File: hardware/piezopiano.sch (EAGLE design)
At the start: 71 parts, among them J1 CON2, J4 JST-PH-2-SMT-SE, Q1 DMN3404L, Q2 DMN3404L, Q3 DMN3404L, Q4 DMN3404L, Q5 DMN3404L, Q6 DMN3404L, Q7 DMN3404L, Q8 DMN3404L, U1 MEGA48A-AU, U2 CH340E_MSOP10, U3 TP4333, Y1 830069392

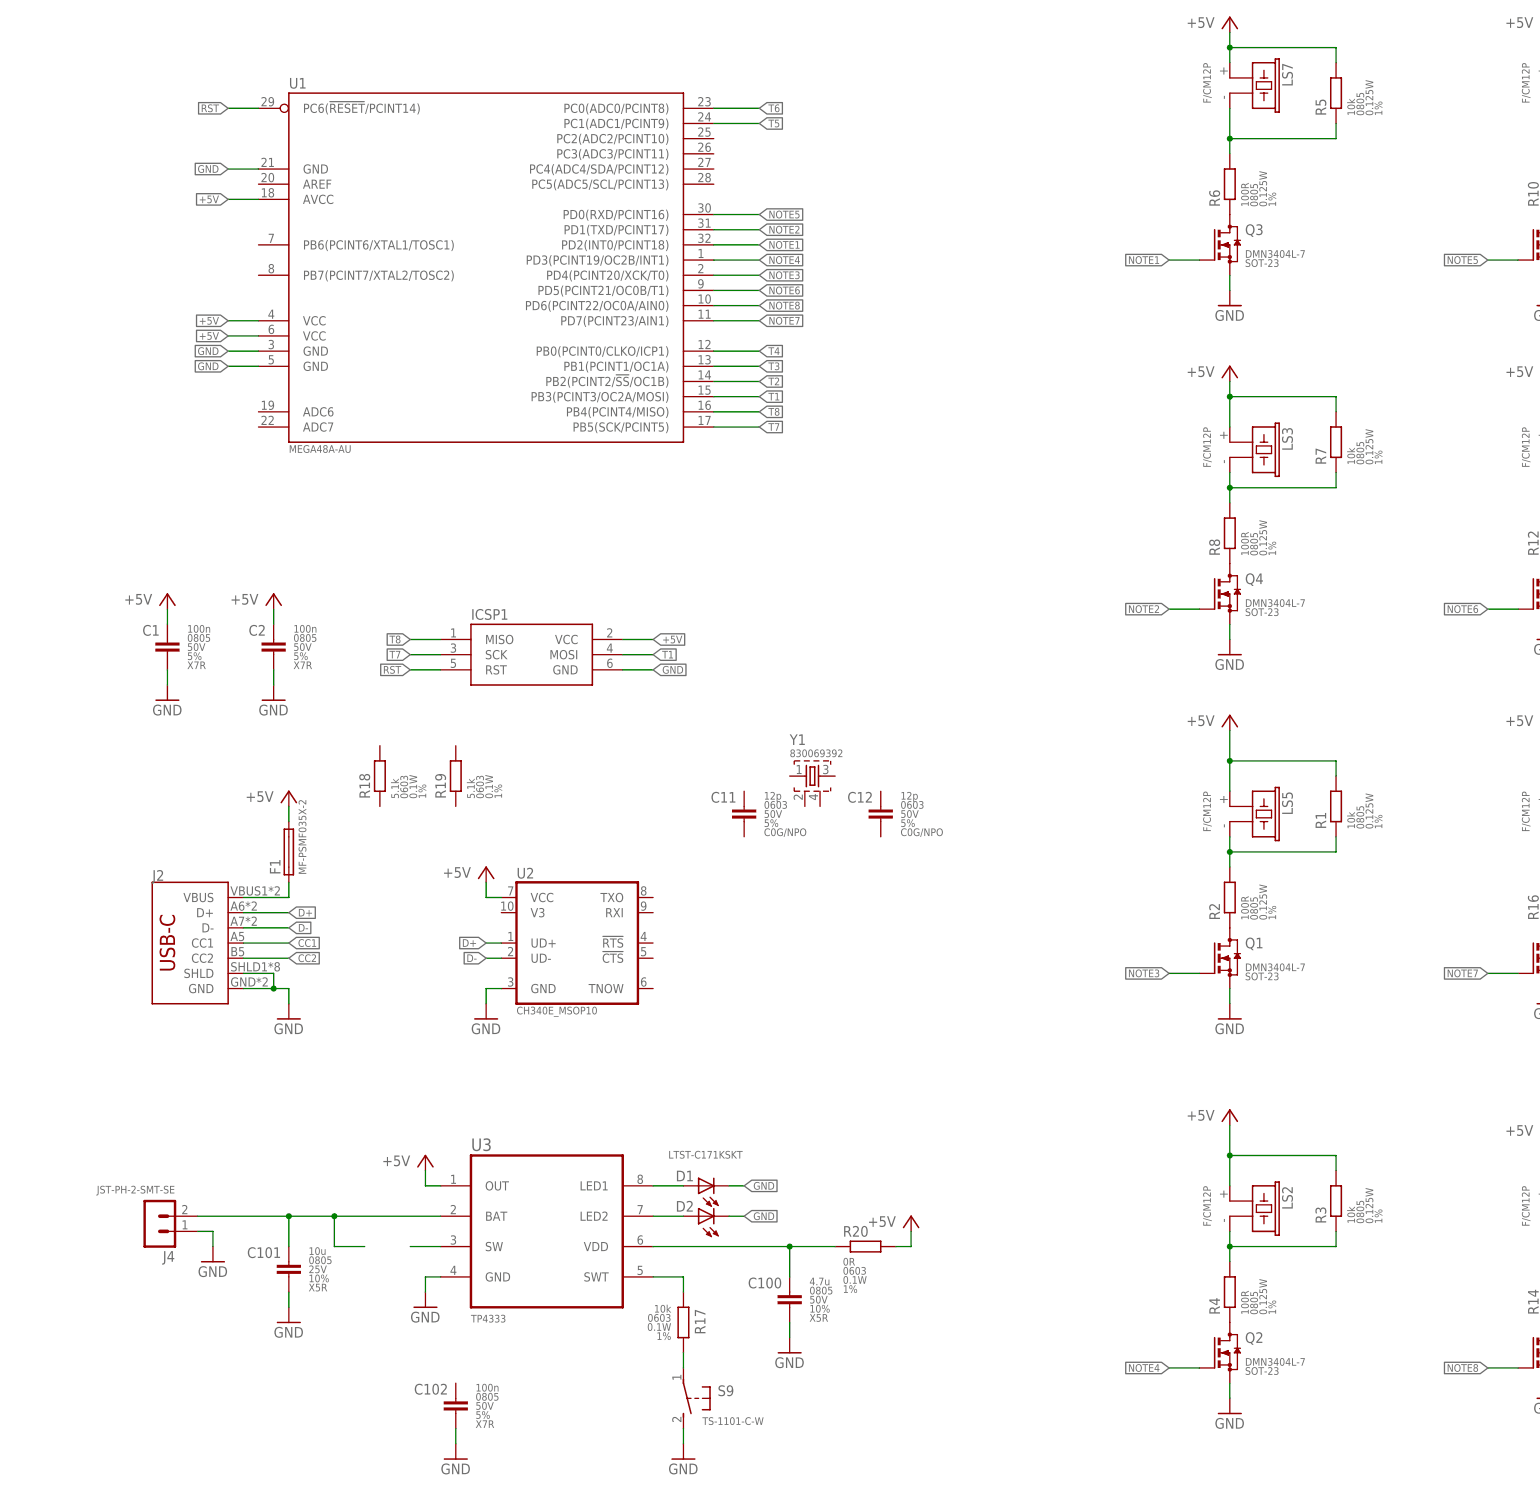
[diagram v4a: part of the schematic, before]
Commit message: Changed to 328 for Arduino support
Changed to ATmega328
Fixed radius from outline
Corrected CH340E
Changed Pinout 328
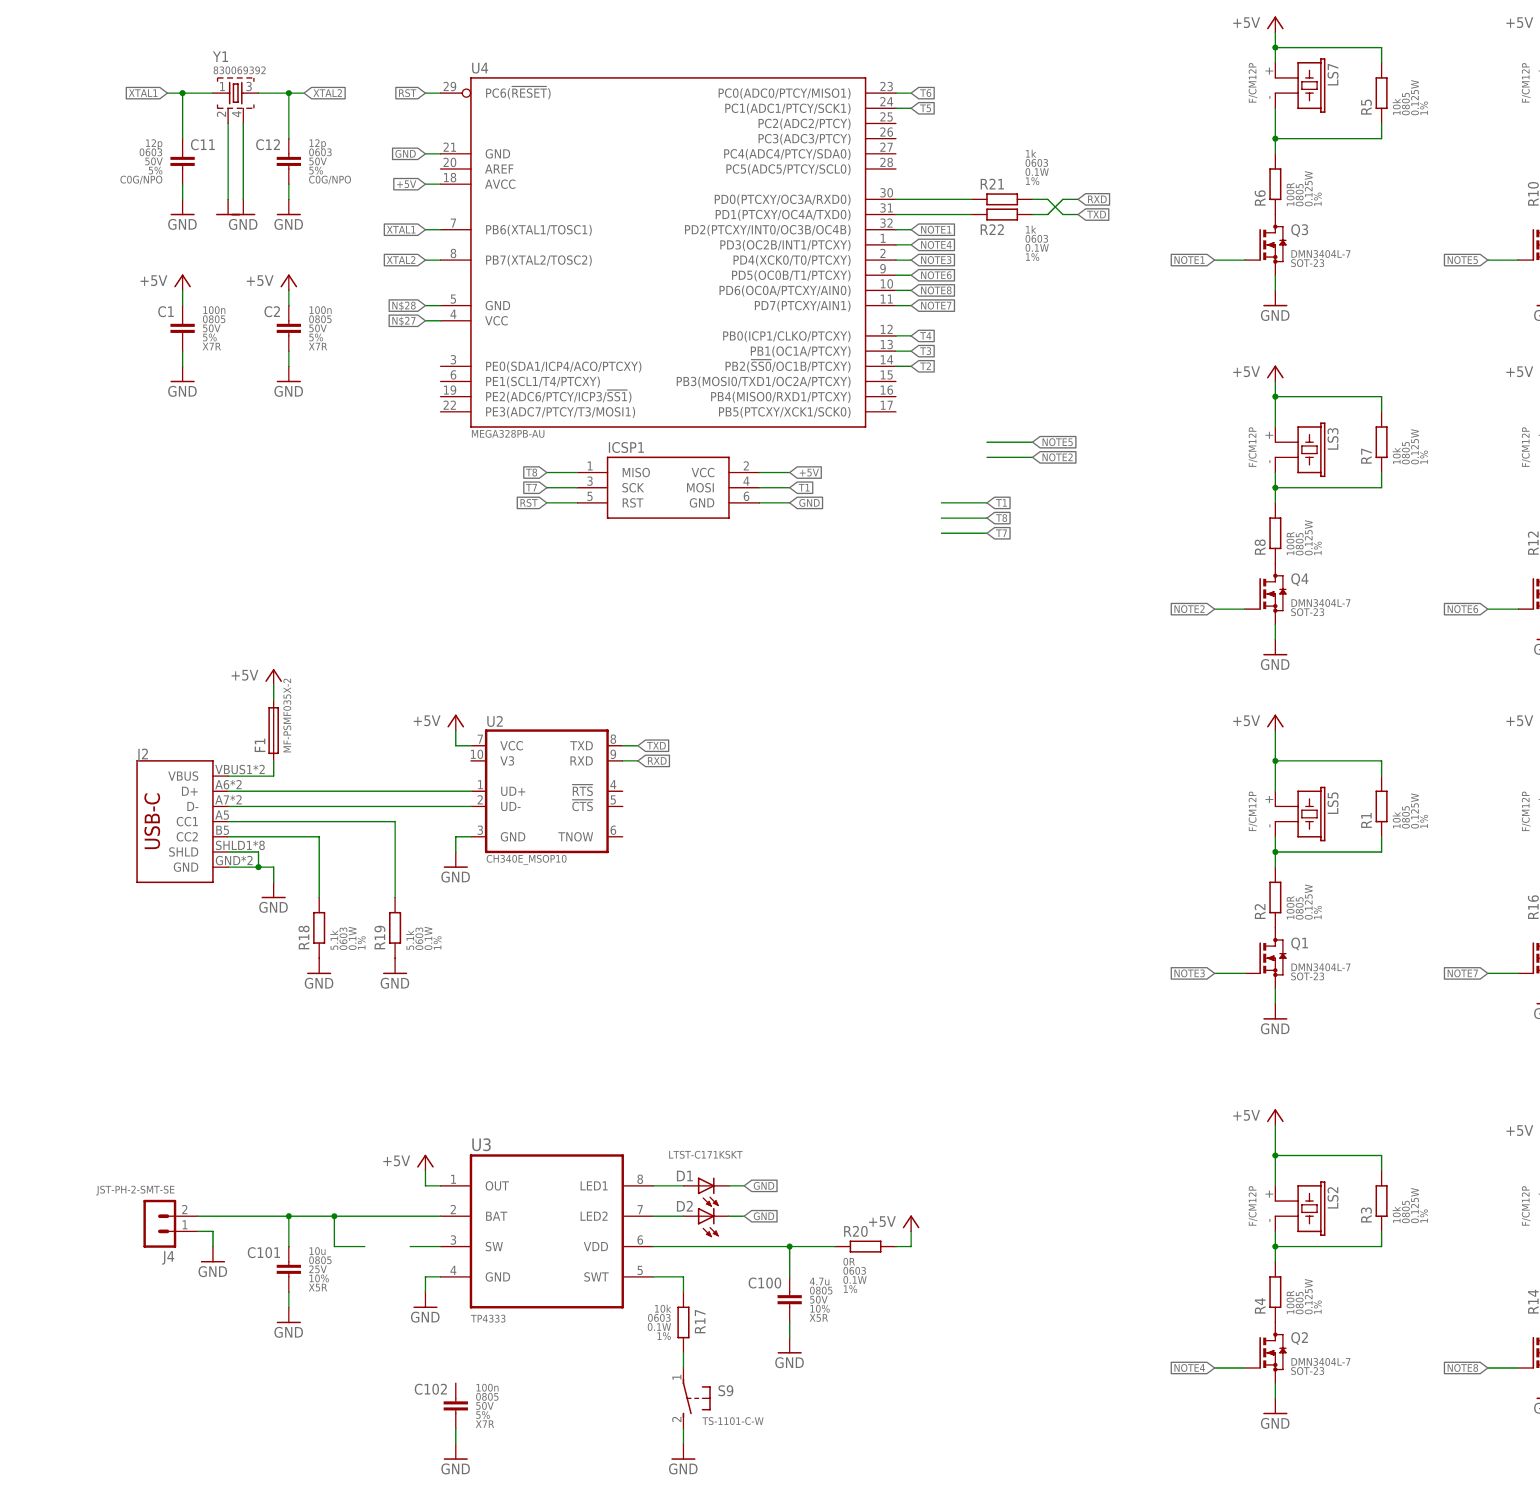
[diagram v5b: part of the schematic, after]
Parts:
- removed U1: MEGA48A-AU, zaan-IC-Microcontroller:MEGA48A-AU
- added R21, R22: 1k, zaan-Resistors:1KOHM-0603-1/10W-1%
- added U4: MEGA328PB-AU, zaan-IC-Microcontroller:MEGA328PB-AU
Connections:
- net D+ renamed N$31
- net D- renamed N$32
- removed net CC1: J2.CC1
- removed net CC2: J2.CC2
- new net N$19: R21.1, U4.PD0(PTCXY/OC3A/RXD0)
- new net N$20: R22.1, U4.PD1(PTCXY/OC4A/TXD0)
- new net N$27: U4.VCC@1
- new net N$28: U4.GND@1
- new net N$29: J2.CC2, R18.2
- new net N$30: J2.CC1, R19.2
- new net RXD: R22.2, U2.RXD
- new net TXD: R21.2, U2.TXD
- new net XTAL1: C11.1, U4.PB6(XTAL1/TOSC1), Y1.1
- new net XTAL2: C12.1, U4.PB7(XTAL2/TOSC2), Y1.3
- net +5V: now also U4.AVCC; no longer U1.AVCC, U1.VCC@1, U1.VCC@2
- net GND: now also C11.2, C12.2, R18.1, R19.1, U4.GND, Y1.2, Y1.4; no longer U1.GND, U1.GND@1, U1.GND@2
- net NOTE1: now also U4.PD2(PTCXY/INT0/OC3B/OC4B); no longer U1.PD2(INT0/PCINT18)
- net NOTE2: no longer U1.PD1(TXD/PCINT17)
- net NOTE3: now also U4.PD4(XCK0/T0/PTCXY); no longer U1.PD4(PCINT20/XCK/T0)
- net NOTE4: now also U4.PD3(OC2B/INT1/PTCXY); no longer U1.PD3(PCINT19/OC2B/INT1)
- net NOTE5: no longer U1.PD0(RXD/PCINT16)
- net NOTE6: now also U4.PD5(OC0B/T1/PTCXY); no longer U1.PD5(PCINT21/OC0B/T1)
- net NOTE7: now also U4.PD7(PTCXY/AIN1); no longer U1.PD7(PCINT23/AIN1)
- net NOTE8: now also U4.PD6(OC0A/PTCXY/AIN0); no longer U1.PD6(PCINT22/OC0A/AIN0)
- net RST: now also U4.PC6(!RESET!); no longer U1.PC6(!RESET!/PCINT14)
- net T1: no longer U1.PB3(PCINT3/OC2A/MOSI)
- net T2: now also U4.PB2(!SS0!/OC1B/PTCXY); no longer U1.PB2(PCINT2/!SS!/OC1B)
- net T3: now also U4.PB1(OC1A/PTCXY); no longer U1.PB1(PCINT1/OC1A)
- net T4: now also U4.PB0(ICP1/CLKO/PTCXY); no longer U1.PB0(PCINT0/CLKO/ICP1)
- net T5: now also U4.PC1(ADC1/PTCY/SCK1); no longer U1.PC1(ADC1/PCINT9)
- net T6: now also U4.PC0(ADC0/PTCY/MISO1); no longer U1.PC0(ADC0/PCINT8)
- net T7: no longer U1.PB5(SCK/PCINT5)
- net T8: no longer U1.PB4(PCINT4/MISO)
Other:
- moved on the sheet: C1, C11, C12, C2, F1, ICSP1, J2, LS2, LS3, LS5, LS7, Q1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

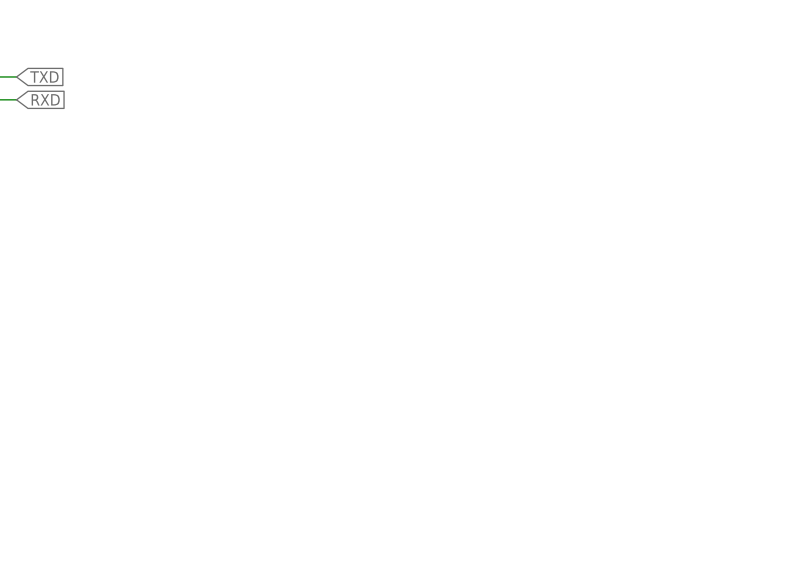
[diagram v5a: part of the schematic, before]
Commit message: Added RGB LED
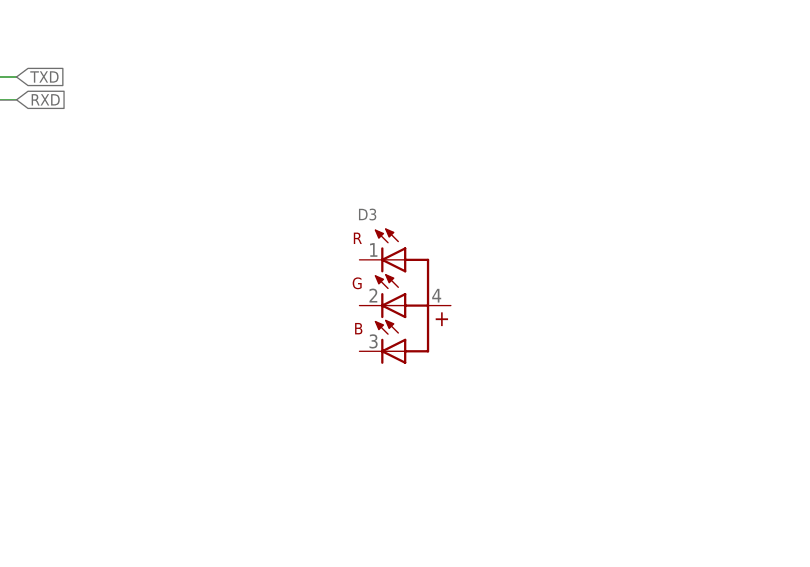
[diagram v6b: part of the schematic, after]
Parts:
- added D3: (no value), zaan-Optoelectronics:150121M173000
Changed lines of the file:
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@@
 <part name="GND40" library="supply1" library_urn="urn:adsk.eagle:library:371" deviceset="GND" device=""/>
 <part name="GND41" library="supply1" library_urn="urn:adsk.eagle:library:371" deviceset="GND" device=""/>
+<part name="D3" library="zaan-Optoelectronics" library_urn="urn:adsk.eagle:library:16759395" deviceset="150121" device="M173000" package3d_urn="urn:adsk.eagle:package:16759422/1"/>
 </parts>
 <sheets>
@@
 <attribute name="VALUE" x="53.34" y="88.9" size="1.778" layer="96"/>
 </instance>
+<instance part="D3" gate="G$1" x="139.7" y="104.14" smashed="yes">
+<attribute name="NAME" x="134.41" y="113.622" size="1.27" layer="95"/>
+<attribute name="VALUE" x="135.07" y="95.772" size="1.27" layer="96"/>
+</instance>
 </instances>

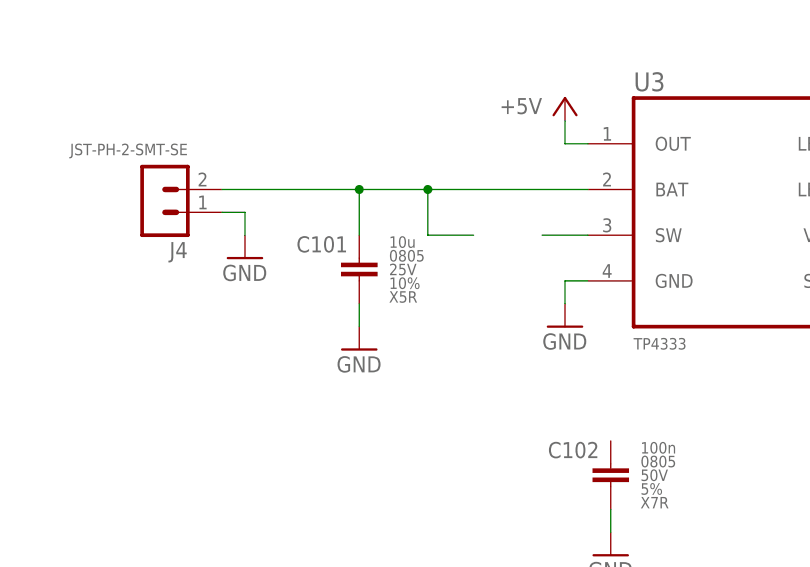
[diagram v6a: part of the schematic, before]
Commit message: Added inductor, corrected LED
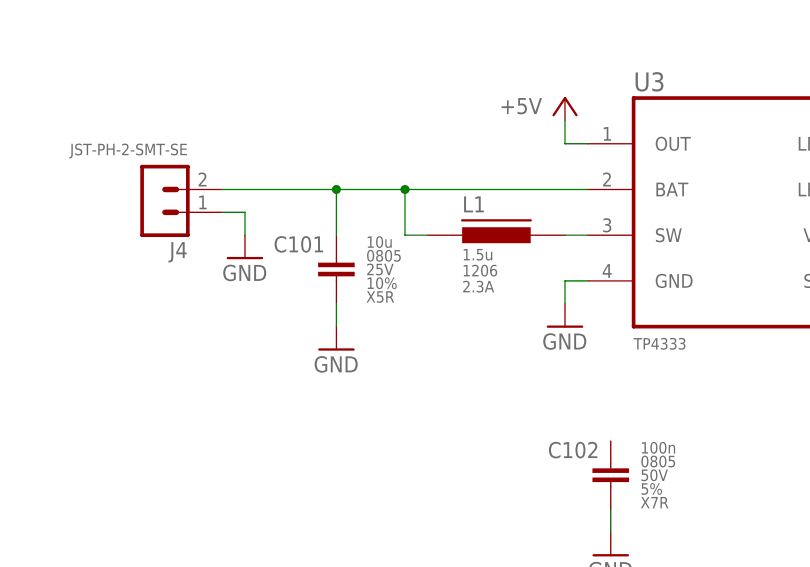
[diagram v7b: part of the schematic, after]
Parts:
- added L1: 1.5u, zaan-Inductors:WE-LQS-L3015-1.5U
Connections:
- net N$21: now also L1.1
- net N$22: now also L1.2
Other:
- moved on the sheet: C101
